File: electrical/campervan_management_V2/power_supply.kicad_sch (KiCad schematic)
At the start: 31 parts, among them Q8 Q_PMOS_DGS, Q9 Q_PMOS_DGS, U1 MCP16311T-E/MNS, U2 AMS1117-3.3, U22 LTV-817S-TA1-C, U23 LTV-817S-TA1-C, U5 AMS1117-3.3

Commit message: updated
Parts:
- R2: footprint Resistor_SMD:R_0805_2012Metric -> Resistor_SMD:R_0603_1608Metric; Extended B -> (none); LCSC PN C17801 -> (none)
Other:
- note added: "Add capacitor for delay when switching batteries"
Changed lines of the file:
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@@
 		)
 	)
+	(text "Add capacitor for delay when switching batteries\n"
+		(exclude_from_sim no)
+		(at 64.77 63.5 0)
+		(effects
+			(font
+				(size 2.54 2.54)
+				(color 255 0 0 1)
+			)
+		)
+	)
 	(text "Battery 1 / Battery 2 Selection"
 		(exclude_from_sim no)
@@
 			)
 		)
-		(property "Footprint" "Resistor_SMD:R_0805_2012Metric"
+		(property "Footprint" "Resistor_SMD:R_0603_1608Metric"
 			(at 228.092 38.1 90)
 			(effects
@@
 			)
 		)
-		(property "LCSC PN" "C17801"
+		(property "LCSC PN" ""
 			(at 229.87 38.1 0)
 			(effects
@@
 			)
 		)
-		(property "Extended" "B"
+		(property "Extended" ""
 			(at 229.87 38.1 0)
 			(effects

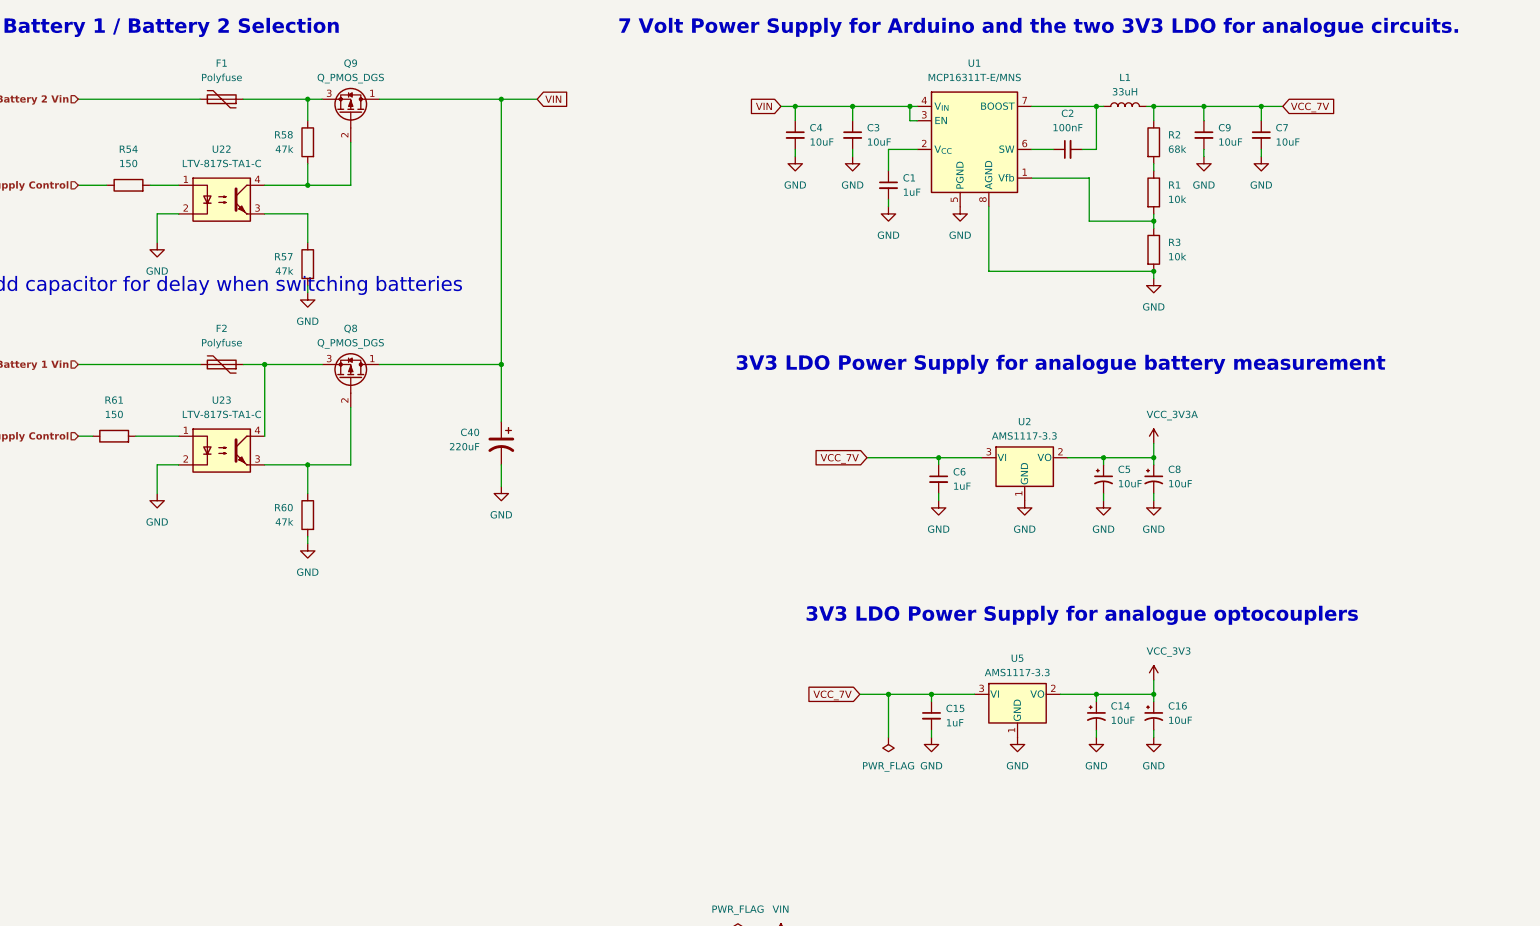
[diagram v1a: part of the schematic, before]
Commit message: First attempt at PCB layout
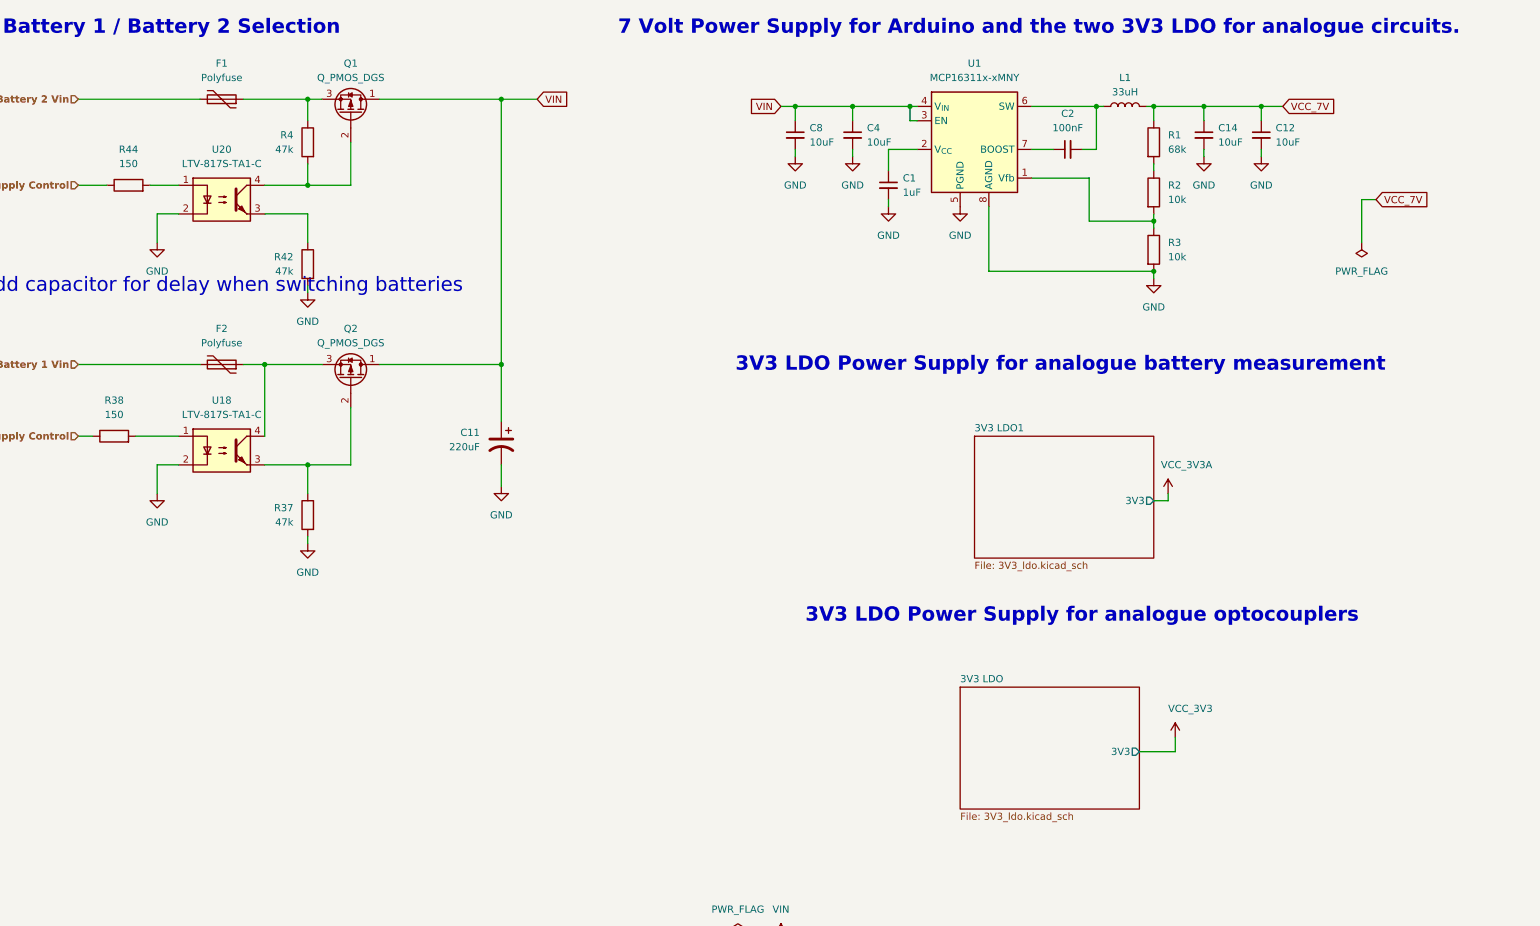
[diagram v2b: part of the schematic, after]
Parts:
- removed C14, C16, C5, C8: 10uF, Capacitor_Tantalum_SMD:CP_EIA-3216-18_Kemet-A, symbol camper_van:C_tantalum
- removed C15, C6: 1uF, Capacitor_SMD:C_0805_2012Metric, symbol Device:C_Small
- removed U2, U5: AMS1117-3.3, CV_connector:SOT-223-3_TabPin1, symbol camper_van:SPX1117
- C1: footprint Capacitor_SMD:C_0805_2012Metric -> Capacitor_SMD:C_0603_1608Metric; LCSC PN C28323 -> C15849
- U1: value MCP16311T-E/MNS -> MCP16311x-xMNY; footprint Package_SO:MSOP-8_3x3mm_P0.65mm -> Package_DFN_QFN:DFN-8-1EP_3x2mm_P0.5mm_EP1.75x1.45mm; Extended E -> (none); LCSC PN C627024 -> (none)
- renumbered C40 to C11, C7 to C12, C9 to C14, C3 to C4, C4 to C8, Q9 to Q1, Q8 to Q2, R2 to R1, R1 to R2, R60 to R37, R61 to R38, R58 to R4, R57 to R42, R54 to R44, U23 to U18, U22 to U20
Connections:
- net GND: now also U1.9 (GND)
- net at C2.2, L1.1: now also U1.6 (SW); no longer U1.7 (BOOST)
- net at C2.1: now also U1.7 (BOOST); no longer U1.6 (SW)
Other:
- added sheet 3V3 LDO (3V3_ldo.kicad_sch)
- added sheet 3V3 LDO1 (3V3_ldo.kicad_sch)

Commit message: Close to final design
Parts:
- removed Q1, Q2: Q_PMOS_DGS, Package_TO_SOT_SMD:SOT-23, symbol Transistor_FET:Q_PMOS_DGS
- removed R42: 47k, Resistor_SMD:R_0805_2012Metric, symbol Device:R
- added C14: 220pF, Capacitor_SMD:C_0805_2012Metric, symbol camper_van:C_SMD_Ceramic_0402
- added D1, D2, D4: 1N418W, Diode_SMD:D_SOD-123, symbol Diode:1N914
- added Q1, Q2: FDS4685, Package_SO:SOIC-8_3.9x4.9mm_P1.27mm, symbol Transistor_FET:FDS9435A
- added R9: 330, Resistor_SMD:R_0805_2012Metric, symbol Device:R
- C11: footprint Capacitor_SMD:CP_Elec_6.3x5.9 -> Capacitor_THT:C_Radial_D6.3mm_H11.0mm_P2.50mm
- F1: renamed from F2; footprint Fuse:Fuseholder_Littelfuse_Nano2_157x -> Fuse:Fuse_1812_4532Metric
- F2: renamed from F1; footprint Fuse:Fuseholder_Littelfuse_Nano2_157x -> Fuse:Fuse_1812_4532Metric
- L2: renamed from L1; JLCPCB (none) -> 2.55; e14 (none) -> 4.65
- R3: renamed from R1; Extended (none) -> B; LCSC PN (none) -> C23231
- R7: renamed from R4; value 47k -> 1k
- R8: renamed from R37; value 47k -> 27k
- U2: renamed from U1; Extended (none) -> E; JLCPCB (none) -> 1.05; LCSC PN (none) -> C510882; e14 (none) -> 3.55
- renumbered C14 to C13, C1 to C3, C2 to C4, C4 to C7, R44 to R11, R38 to R12, R2 to R5, R3 to R6, U20 to U3, U18 to U4
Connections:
- net GND: now also U3.3, C14.1, R9.1
- net VIN: now also Q1.5 (D), Q1.6 (D), Q1.7 (D), Q1.8 (D), Q2.5 (D), Q2.6 (D), Q2.7 (D), Q2.8 (D)
- net at F2.1: now also D1.2 (A), Q2.1 (S), Q2.2 (S), Q2.3 (S); no longer R7.1
- net at R8.1, U4.3: now also Q1.4 (G)
- net at F1.1: now also D2.2 (A), Q1.1 (S), Q1.2 (S), Q1.3 (S); no longer U4.4
- net at R11.2, U3.1: now also D4.2 (A)
- net at R7.2, U3.4: now also Q2.4 (G)
- new net: C14.2, D4.1 (K), R9.2
- new net Vps: D1.1 (K), D2.1 (K), R7.1, U4.4
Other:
- note added: "3V3 LDO Power Supplies"
- note added: "Analogue Optocouplers"
- note added: "Battery Measurement"
- note removed: "3V3 LDO Power Supply for analogue battery measurement"
- note removed: "3V3 LDO Power Supply for analogue optocouplers"
- note removed: "Add capacitor for delay when switching batteries"
- moved on the sheet: C11, C12, C13, C3, C4, C7, C8, F1, F2, L2, R11, R12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
